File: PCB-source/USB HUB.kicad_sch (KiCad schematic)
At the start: 13 parts, among them U302 CH334P, Y900 Crystal_GND24

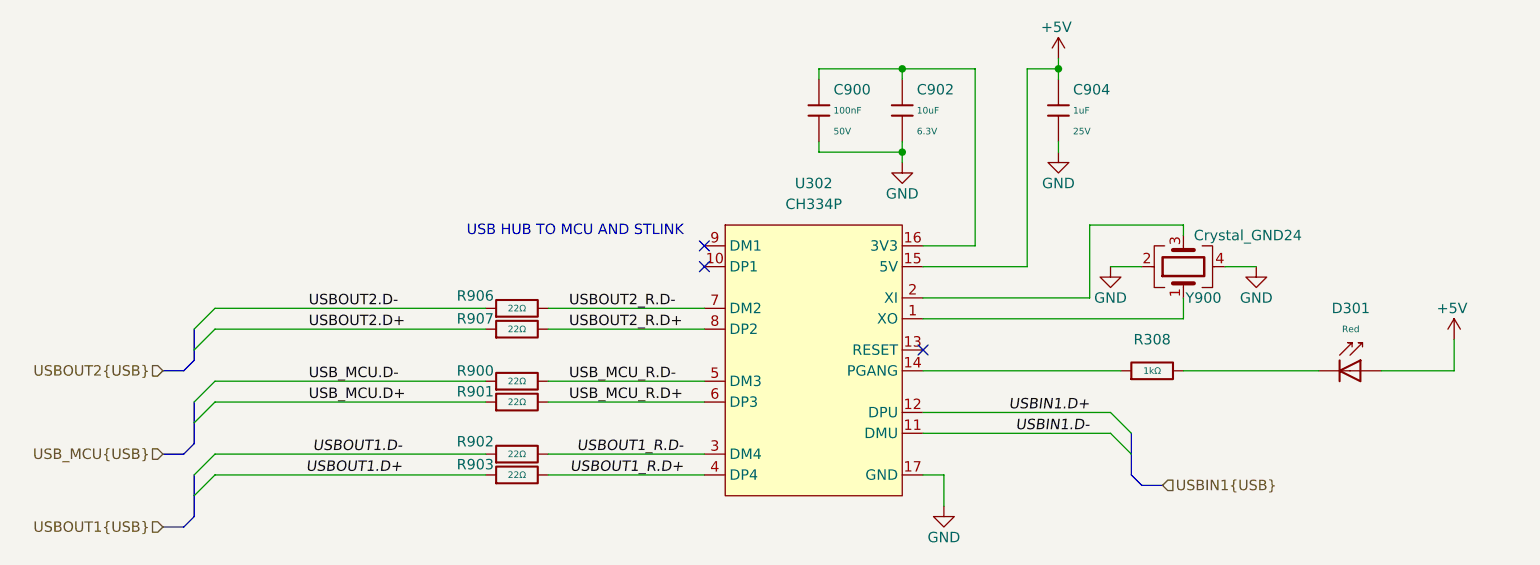
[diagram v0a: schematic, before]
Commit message: Finish component and diffpair placement
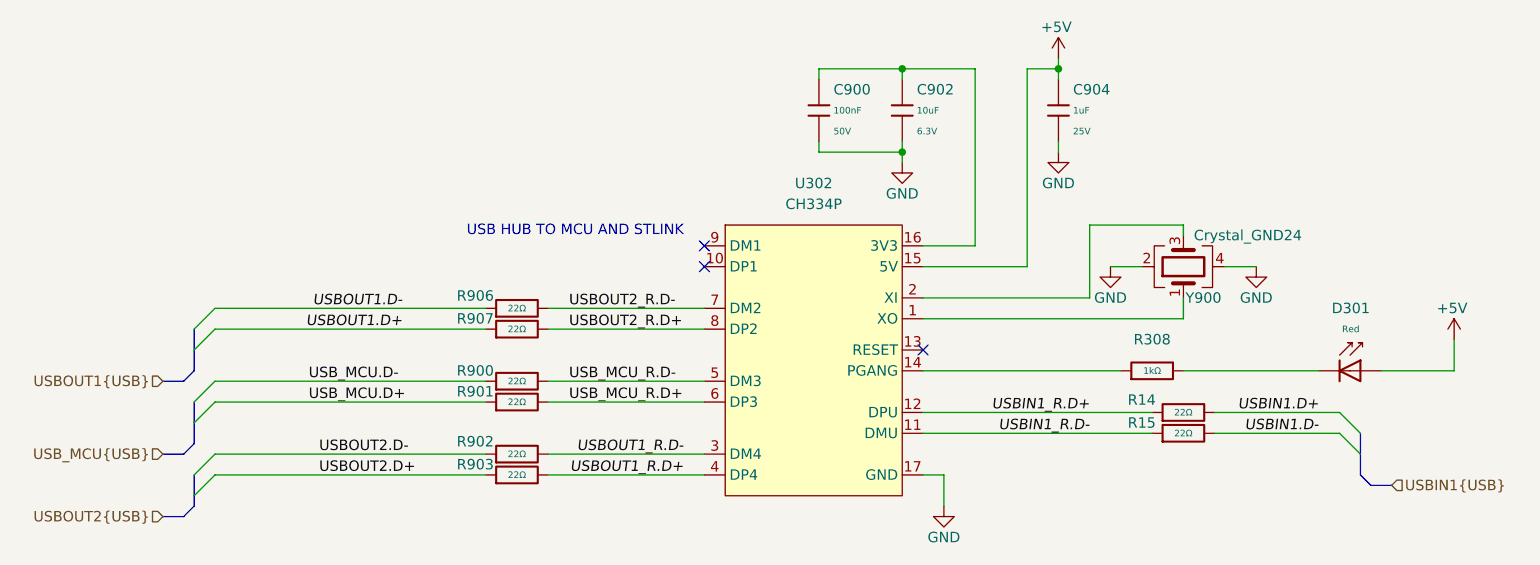
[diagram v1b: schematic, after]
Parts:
- added R14, R15: 22Ω, PCM_JLCPCB:R_0402, symbol PCM_JLCPCB-Resistors:0402,22Ω
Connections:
- net USBIN1.D+: now also R14.2; no longer U302.12 (DPU)
- net USBIN1.D-: now also R15.2; no longer U302.11 (DMU)
- net USBOUT1.D+: now also R907.1; no longer R903.1
- net USBOUT1.D-: now also R906.1; no longer R902.1
- net USBOUT2.D+: now also R903.1; no longer R907.1
- net USBOUT2.D-: now also R902.1; no longer R906.1
- new net USBIN1_R.D+: R14.1, U302.12 (DPU)
- new net USBIN1_R.D-: R15.1, U302.11 (DMU)
